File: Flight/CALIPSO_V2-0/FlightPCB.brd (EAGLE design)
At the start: 63.6 x 94.9 mm, 65 parts, among them M1 MOSFET_60V_22A, M2 MOSFET_60V_22A, M3 MOSFET_60V_22A, M4 MOSFET_60V_22A, M5 MOSFET_60V_22A, M5V MOSFET_60V_22A, T4.1_L 24p, T4.1_R 24p

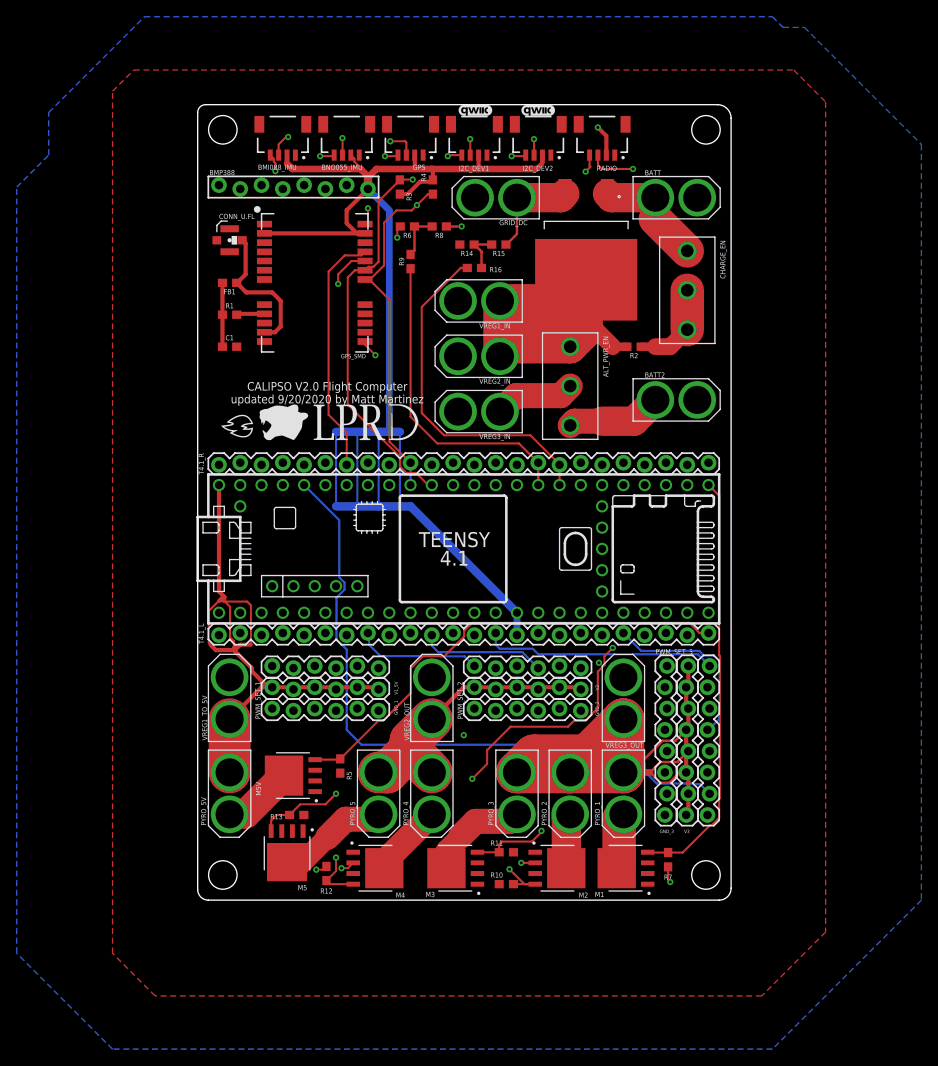
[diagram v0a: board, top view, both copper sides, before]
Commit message: MFG Files
Includes PDFs and CSV files for parts... PCB file is no longer ready to order as it has to be re-routed
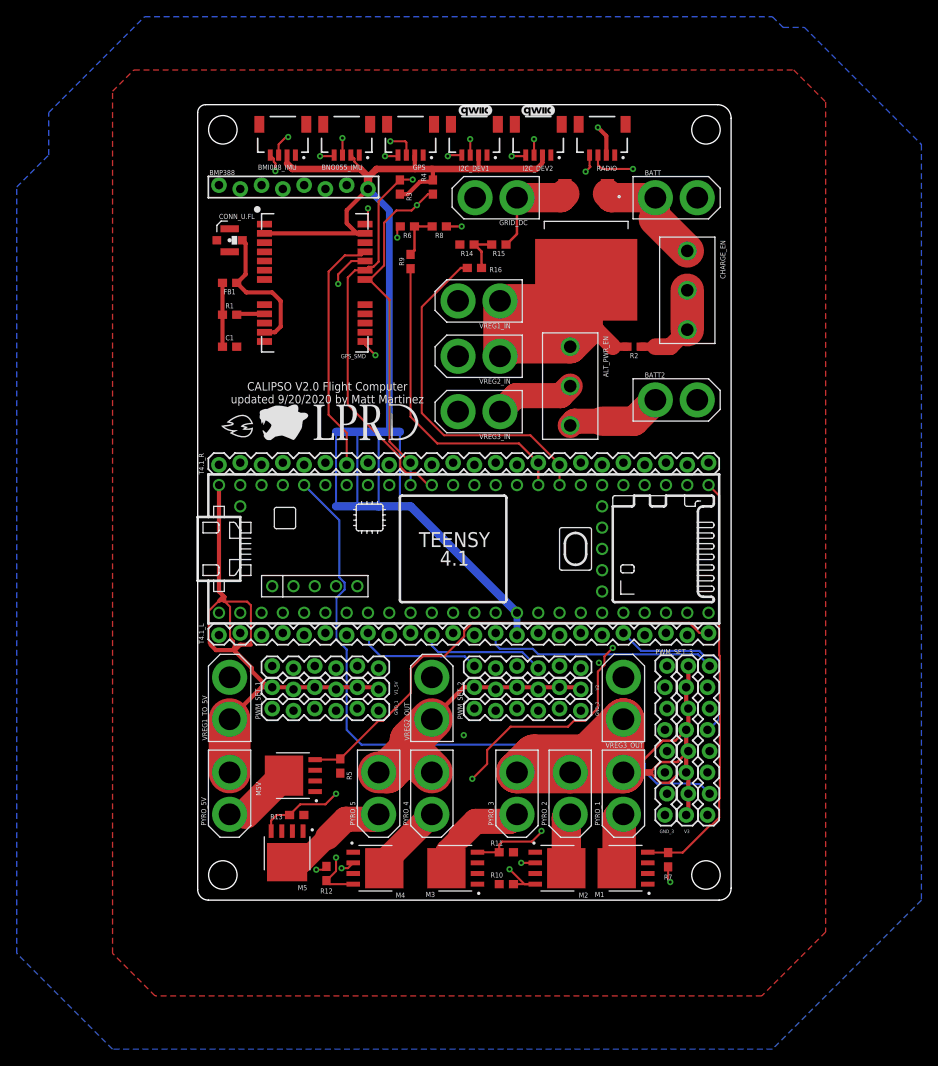
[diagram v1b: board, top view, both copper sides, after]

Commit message: Unsaved changes after 10/11/2020
changes that I made after 10/11/2020. I don't recall what all the changes are, but I will look soon.
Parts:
- LOGO1, LOGO2: value QWIIC_LOGO_4MM -> QWIIC_LOGO_CONNECTOR; device SparkFun-Aesthetics:QWIIC_4MM -> SparkFun-Aesthetics:QWIIC_5.5MM
- moved LOGO2 2.41 mm to (33.1, 101.7)
- moved LOGO1 2.40 mm to (41.9, 101.3)
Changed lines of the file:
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@@
 </layers>
 <board>
-<fusionsync huburn="a.YnVzaW5lc3M6bXl1bW4xNzk" projecturn="a.YnVzaW5lc3M6bXl1bW4xNzkjRDIwMTkwNzA2MjAyMzIxMDMx" f3durn="urn:adsk.wipprod:dm.lineage:VqhNx6DGQo228uV-65ZaWg" pcbguid="" lastpulledtime="" lastsyncedchangeguid="" latestrevisionid="06cb4512-8221-4e09-8c76-3a624050dc2e" lastsyncedrevisionid="06cb4512-8221-4e09-8c76-3a624050dc2e" lastboardhashguid="36d0bf69-8a66-7bb8-8a8f-f5e464f03517" lastpushedtime="2020-09-28T01:03:13Z" linktopcb3d="false"/>
+<fusionsync huburn="a.YnVzaW5lc3M6bXl1bW4xNzk" projecturn="a.YnVzaW5lc3M6bXl1bW4xNzkjRDIwMTkwNzA2MjAyMzIxMDMx" f3durn="urn:adsk.wipprod:dm.lineage:VqhNx6DGQo228uV-65ZaWg" pcbguid="" lastpulledtime="" lastsyncedchangeguid="" latestrevisionid="06cb4512-8221-4e09-8c76-3a624050dc2e" lastsyncedrevisionid="06cb4512-8221-4e09-8c76-3a624050dc2e" lastboardhashguid="36d0bf69-8a66-7bb8-8a8f-f5e464f03517" lastpushedtime="2020-09-28T01:03:13Z" linktopcb3d="true"/>
 <plain>
 <text x="15.466" y="65.628" size="1.016" layer="21" align="center">CALIPSO V2.0 Flight Computer
@@
 <attribute name="VALUE" x="10.922" y="16.002" size="0.6096" layer="27" font="vector" ratio="20" rot="R180" align="top-center"/>
 </element>
-<element name="LOGO1" library="SparkFun-Aesthetics" package="QWIIC_4MM" value="QWIIC_LOGO_4MM" x="40.64" y="99.314" smashed="yes"/>
-<element name="LOGO2" library="SparkFun-Aesthetics" package="QWIIC_4MM" value="QWIIC_LOGO_4MM" x="33.147" y="99.314" smashed="yes"/>
+<element name="LOGO1" library="SparkFun-Aesthetics" package="QWIIC_5.5MM" value="QWIIC_LOGO_CONNECTOR" x="41.91" y="101.346" smashed="yes"/>
+<element name="LOGO2" library="SparkFun-Aesthetics" package="QWIIC_5.5MM" value="QWIIC_LOGO_CONNECTOR" x="33.147" y="101.727" smashed="yes"/>
 <element name="R14" library="SparkFun-Resistors" package="0603" value="1k" x="32.131" y="83.312" smashed="yes" rot="R180">
 <attribute name="NAME" x="32.131" y="82.55" size="0.6096" layer="25" font="vector" ratio="20" rot="R180" align="bottom-center"/>
